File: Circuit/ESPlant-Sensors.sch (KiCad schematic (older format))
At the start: 6 parts, among them U301 BME280, U302 ADXL345

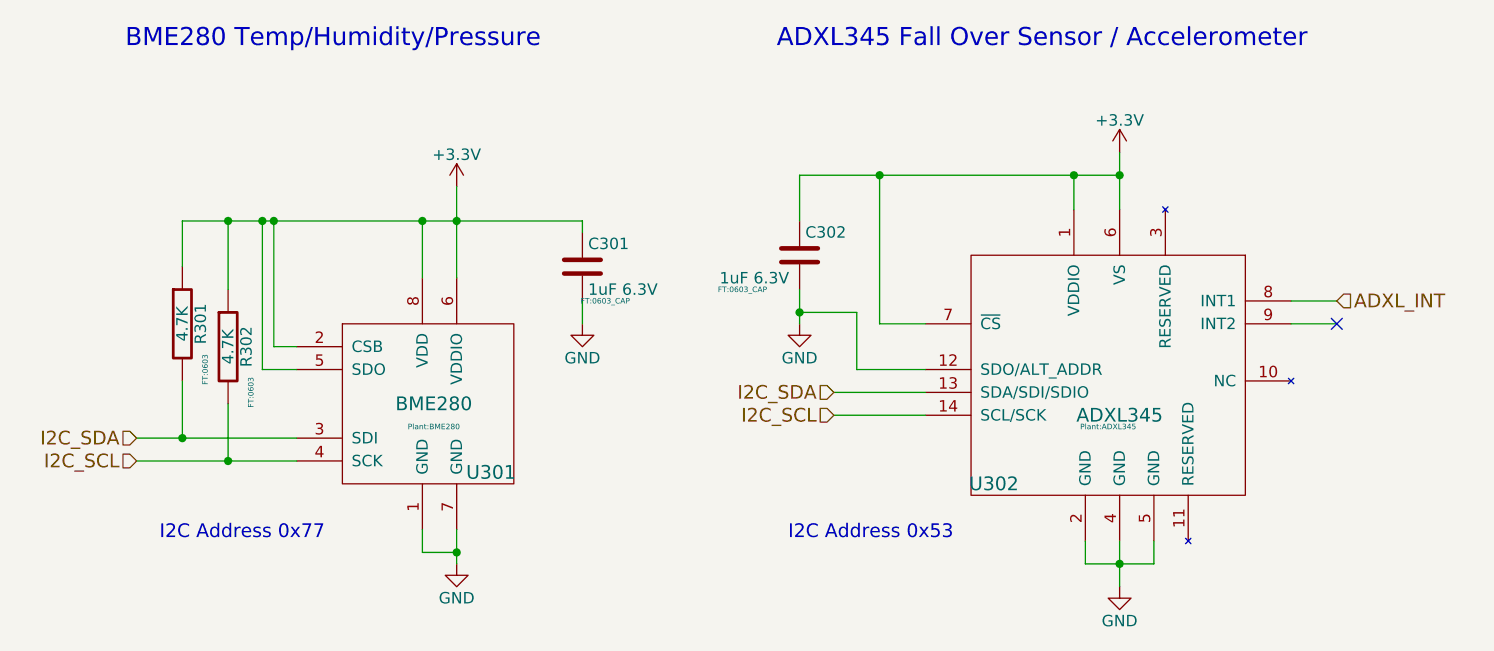
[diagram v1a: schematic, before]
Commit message: Fix silkscreen & slot width issues noted by @hackvana, bump version V1.3
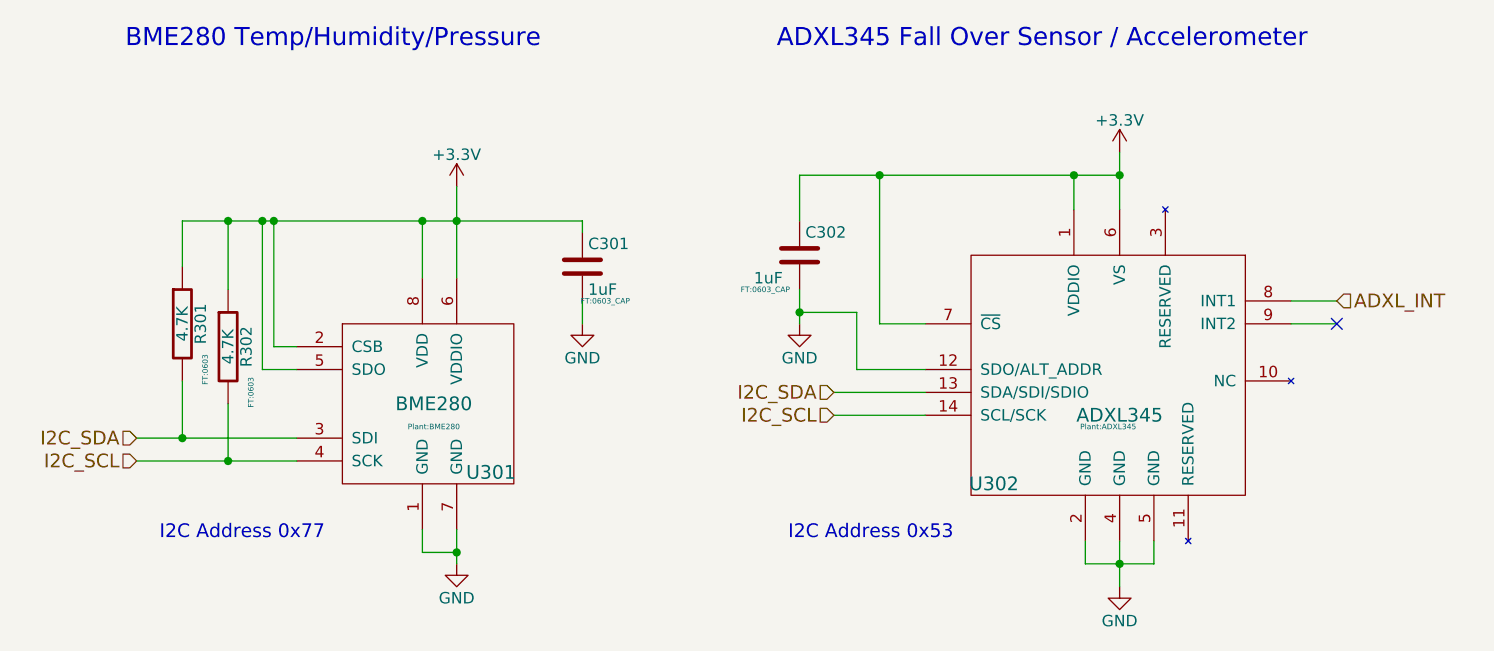
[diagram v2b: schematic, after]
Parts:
- C301, C302: value 1uF 6.3V -> 1uF
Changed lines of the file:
@@
 P 4750 2650
 F 0 "C302" H 4775 2750 50  0000 L CNN
-F 1 "1uF 6.3V" H 4400 2550 50  0000 L CNN
-F 2 "FT:0603_CAP" H 4500 2500 24  0000 C CNN
+F 1 "1uF" H 4550 2550 50  0000 L CNN
+F 2 "FT:0603_CAP" H 4600 2500 24  0000 C CNN
 F 3 "" H 4750 2650 60  0000 C CNN
 	1    4750 2650
@@
 P 3800 2700
 F 0 "C301" H 3825 2800 50  0000 L CNN
-F 1 "1uF 6.3V" H 3825 2600 50  0000 L CNN
+F 1 "1uF" H 3825 2600 50  0000 L CNN
 F 2 "FT:0603_CAP" H 3900 2550 24  0000 C CNN
 F 3 "" H 3800 2700 60  0000 C CNN
